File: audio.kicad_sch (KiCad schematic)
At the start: 36 parts, among them IC10 LM386

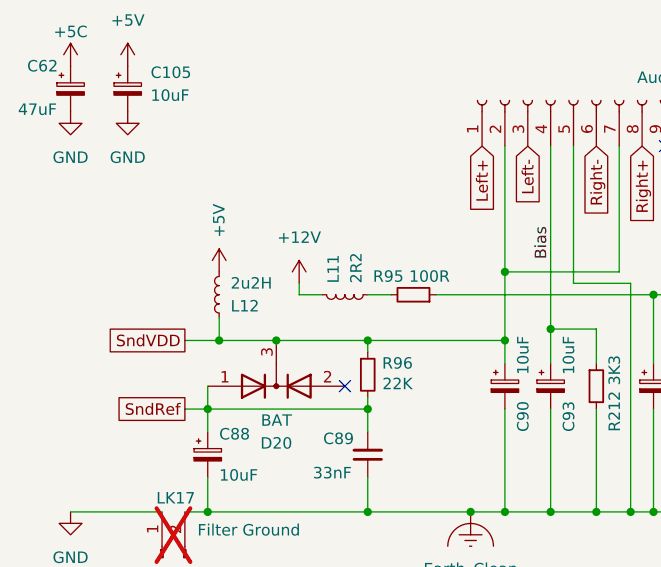
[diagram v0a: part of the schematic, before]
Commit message: fix incorrect value for L12
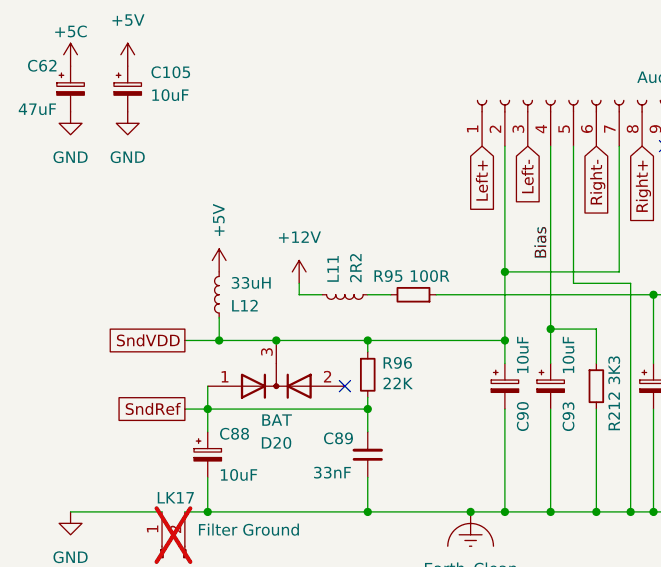
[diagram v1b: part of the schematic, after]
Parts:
- L12: value 2u2H -> 33uH
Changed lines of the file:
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@@
 			)
 		)
-		(property "Value" "2u2H"
+		(property "Value" "33uH"
 			(at 81.28 96.5201 0)
 			(effects

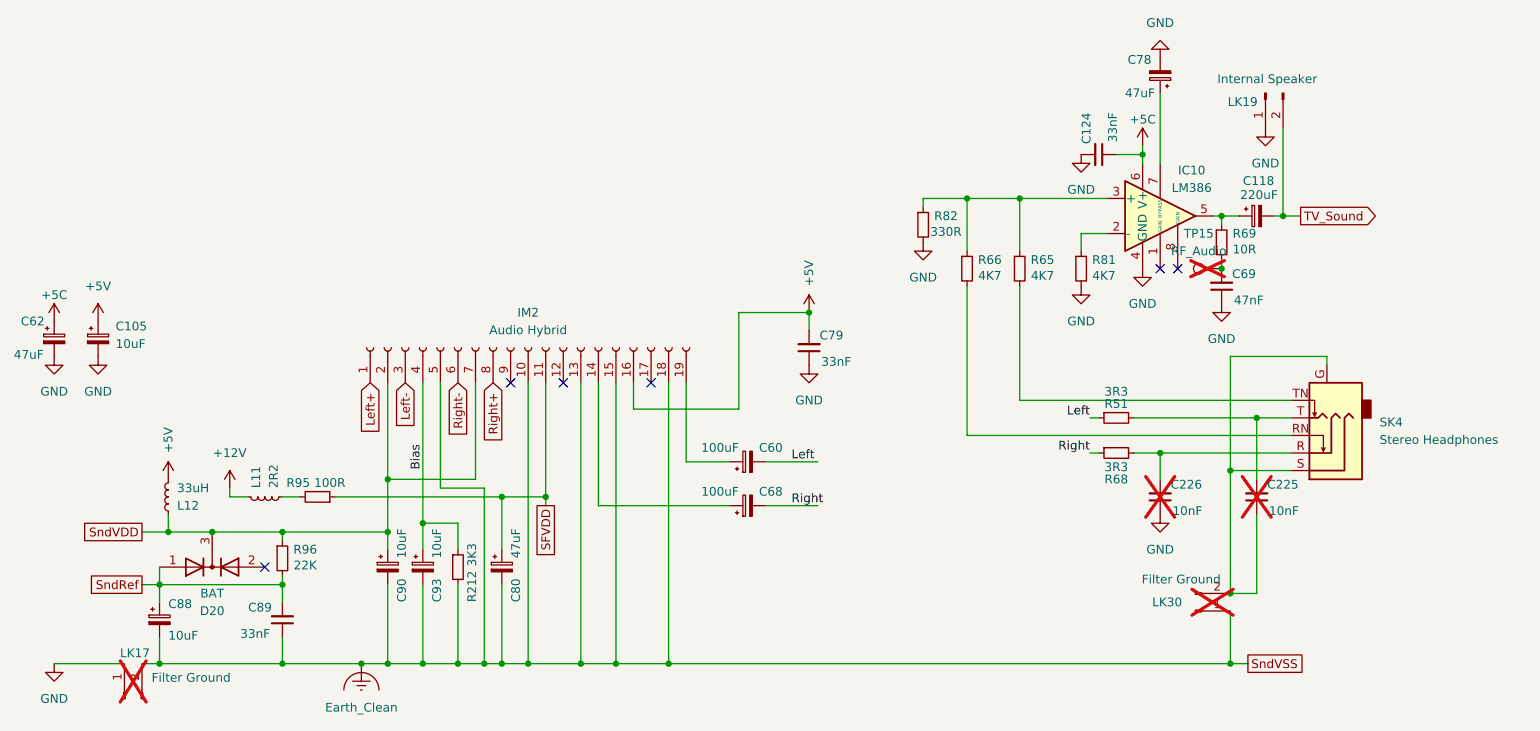
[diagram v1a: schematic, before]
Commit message: verify all component values vs TRM
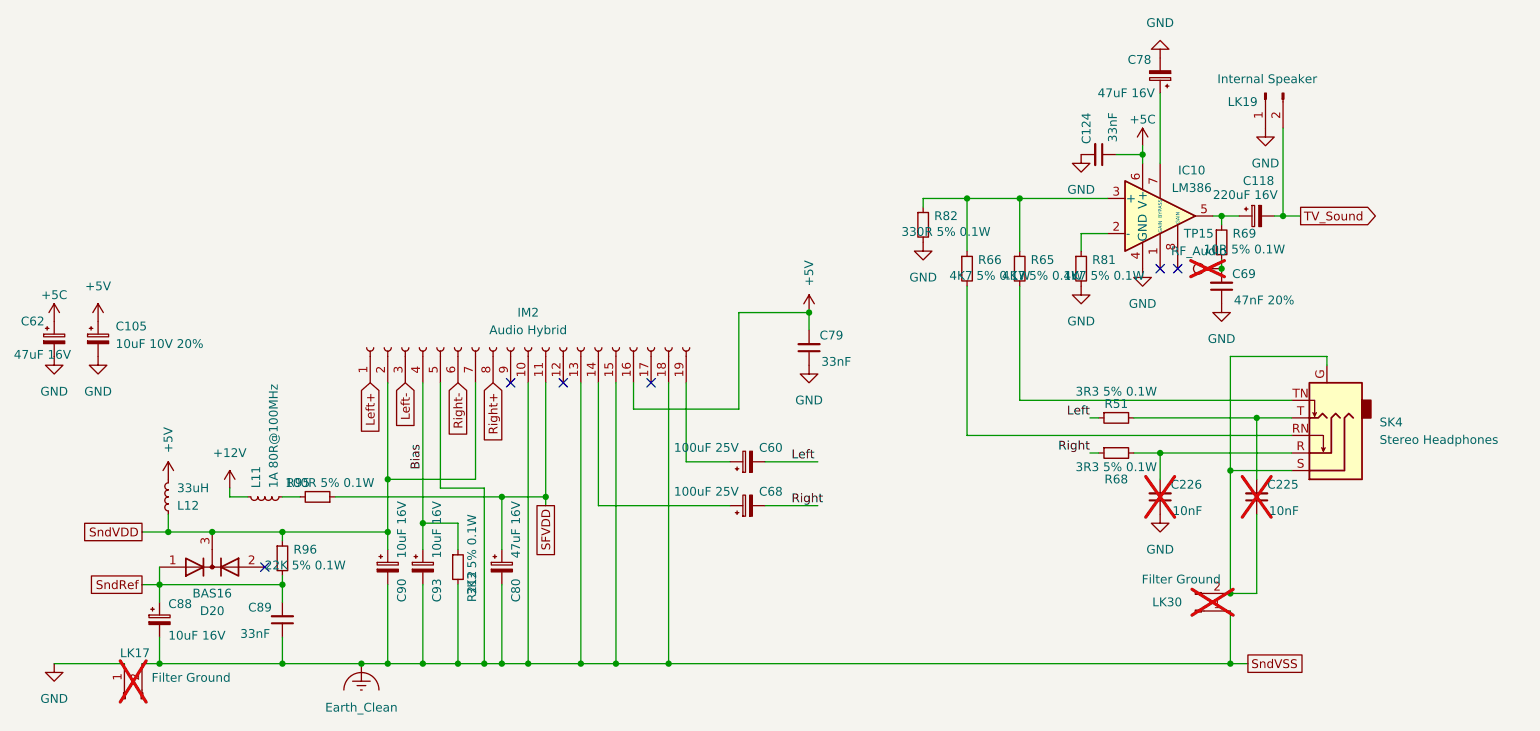
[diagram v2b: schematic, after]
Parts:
- C105: value 10uF -> 10uF 10V 20%
- C118: value 220uF -> 220uF 16V
- C60, C68: value 100uF -> 100uF 25V
- C62, C78, C80: value 47uF -> 47uF 16V
- C69: value 47nF -> 47nF 20%
- C88, C90, C93: value 10uF -> 10uF 16V
- D20: value BAT -> BAS16
- L11: value 2R2 -> 1A 80R@100MHz
- R212: value 3K3 -> 3K3 5% 0.1W
- R51, R68: value 3R3 -> 3R3 5% 0.1W
- R65, R66, R81: value 4K7 -> 4K7 5% 0.1W
- R69: value 10R -> 10R 5% 0.1W
- R82: value 330R -> 330R 5% 0.1W
- R95: value 100R -> 100R 5% 0.1W
- R96: value 22K -> 22K 5% 0.1W
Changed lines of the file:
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@@
 			)
 		)
-		(property "Value" "100uF"
+		(property "Value" "100uF 25V"
 			(at 162.56 90.678 90)
 			(effects
@@
 			)
 		)
-		(property "Value" "10uF"
+		(property "Value" "10uF 10V 20%"
 			(at 72.39 75.6538 0)
 			(effects
@@
 			)
 		)
-		(property "Value" "100uF"
+		(property "Value" "100uF 25V"
 			(at 162.56 97.028 90)
 			(effects
@@
 			)
 		)
-		(property "Value" "22K"
+		(property "Value" "22K 5% 0.1W"
 			(at 99.822 107.696 0)
 			(effects
@@
 			)
 		)
-		(property "Value" "47nF"
+		(property "Value" "47nF 20%"
 			(at 234.188 69.342 0)
 			(effects
@@
 			)
 		)
-		(property "Value" "100R"
+		(property "Value" "100R 5% 0.1W"
 			(at 103.378 95.758 90)
 			(effects
@@
 			)
 		)
-		(property "Value" "2R2"
+		(property "Value" "1A 80R@100MHz"
 			(at 95.2499 96.52 0)
 			(effects
@@
 			)
 		)
-		(property "Value" "4K7"
+		(property "Value" "4K7 5% 0.1W"
 			(at 206.502 65.786 0)
 			(effects
@@
 			)
 		)
-		(property "Value" "220uF"
+		(property "Value" "220uF 16V"
 			(at 240.538 54.102 90)
 			(effects
@@
 			)
 		)
-		(property "Value" "4K7"
+		(property "Value" "4K7 5% 0.1W"
 			(at 198.882 65.786 0)
 			(effects
@@
 			)
 		)
-		(property "Value" "3R3"
+		(property "Value" "3R3 5% 0.1W"
 			(at 217.17 82.55 90)
 			(effects
@@
 			)
 		)
-		(property "Value" "10uF"
+		(property "Value" "10uF 16V"
 			(at 80.01 117.856 0)
 			(effects
@@
 			)
 		)
-		(property "Value" "330R"
+		(property "Value" "330R 5% 0.1W"
 			(at 192.532 59.436 0)
 			(effects
@@
 			)
 		)
-		(property "Value" "47uF"
+		(property "Value" "47uF 16V"
 			(at 57.658 77.216 0)
 			(effects
@@
 			)
 		)
-		(property "Value" "10uF"
+		(property "Value" "10uF 16V"
 			(at 118.872 106.68 90)
 			(effects
@@
 			)
 		)
-		(property "Value" "3K3"
+		(property "Value" "3K3 5% 0.1W"
 			(at 123.952 106.172 90)
 			(effects
@@
 			)
 		)
-		(property "Value" "47uF"
+		(property "Value" "47uF 16V"
 			(at 130.302 106.68 90)
 			(effects
@@
 			)
 		)
-		(property "Value" "47uF"
+		(property "Value" "47uF 16V"
 			(at 222.758 39.37 0)
 			(effects
@@
 			)
 		)
-		(property "Value" "BAT"
+		(property "Value" "BAS16"
 			(at 86.36 111.76 0)
 			(effects
@@
 			)
 		)
-		(property "Value" "10R"
+		(property "Value" "10R 5% 0.1W"
 			(at 235.712 61.976 0)
 			(effects
@@
 			)
 		)
-		(property "Value" "10uF"
+		(property "Value" "10uF 16V"
 			(at 113.792 106.68 90)
 			(effects
@@
 			)
 		)
-		(property "Value" "3R3"
+		(property "Value" "3R3 5% 0.1W"
 			(at 217.17 93.472 90)
 			(effects
@@
 			)
 		)
-		(property "Value" "4K7"
+		(property "Value" "4K7 5% 0.1W"
 			(at 215.392 65.786 0)
 			(effects

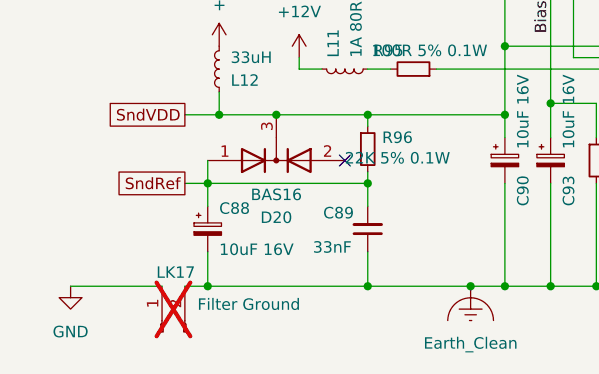
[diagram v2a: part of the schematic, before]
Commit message: switch links to net ties
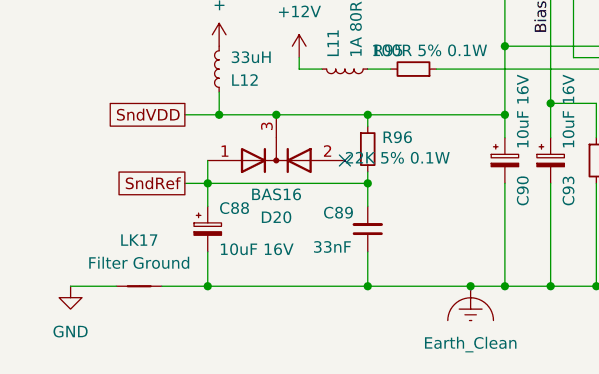
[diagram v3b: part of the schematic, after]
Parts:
- removed LK17: Filter Ground, Connector_PinHeader_2.54mm:PinHeader_1x02_P2.54mm_Vertical, symbol Connector:Conn_01x02_Pin
- added LK17: Filter Ground, Acorn:Link_Connected, symbol Device:NetTie_2
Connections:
- net Earth_Clean: now also LK17.2
- net GND: now also LK17.1
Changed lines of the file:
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@@
 	(wire
 		(pts
-			(xy 76.2 121.92) (xy 78.74 121.92)
+			(xy 73.66 121.92) (xy 78.74 121.92)
 		)
 		(stroke
@@
 	(wire
 		(pts
-			(xy 63.5 121.92) (xy 73.66 121.92)
+			(xy 63.5 121.92) (xy 68.58 121.92)
 		)
 		(stroke
@@
 	)
 	(symbol
-		(lib_id "Connector:Conn_01x02_Pin")
-		(at 73.66 127 90)
-		(unit 1)
-		(exclude_from_sim no)
-		(in_bom yes)
-		(on_board yes)
-		(dnp yes)
-		(property "Reference" "LK17"
-			(at 75.184 120.396 90)
-			(effects
-				(font
-					(size 1.27 1.27)
-				)
-			)
-		)
-		(property "Value" "Filter Ground"
-			(at 83.312 123.952 90)
-			(effects
-				(font
-					(size 1.27 1.27)
-				)
-			)
-		)
-		(property "Footprint" "Connector_PinHeader_2.54mm:PinHeader_1x02_P2.54mm_Vertical"
-			(at 73.66 127 0)
-			(effects
-				(font
-					(size 1.27 1.27)
-				)
-				(hide yes)
-			)
-		)
-		(property "Datasheet" "~"
-			(at 73.66 127 0)
-			(effects
-				(font
-					(size 1.27 1.27)
-				)
-				(hide yes)
-			)
-		)
-		(property "Description" "Generic connector, single row, 01x02, script generated"
-			(at 73.66 127 0)
-			(effects
-				(font
-					(size 1.27 1.27)
-				)
-				(hide yes)
-			)
-		)
-		(pin "2"
-		)
-		(pin "1"
-		)
-		(instances
-			(project "Acorn-A3010"
-				(path "/999882f3-94f8-4a89-9093-27a47d0cb289/0f9e4e4c-7eae-43dc-ad37-0c70003f4236"
-					(reference "LK17")
-					(unit 1)
-				)
-			)
-		)
-	)
-	(symbol
 		(lib_id "power:Earth_Clean")
 		(at 107.95 121.92 0)
@@
 					(unit 1)
 				)
+			)
+		)
+	)
+	(symbol
+		(lib_id "Device:NetTie_2")
+		(at 71.12 121.92 0)
+		(unit 1)
+		(exclude_from_sim no)
+		(in_bom no)
+		(on_board yes)
+		(dnp no)
+		(fields_autoplaced yes)
+		(property "Reference" "LK17"
+			(at 71.12 116.84 0)
+			(effects
+				(font
+					(size 1.27 1.27)
+				)
+			)
+		)
+		(property "Value" "Filter Ground"
+			(at 71.12 119.38 0)
+			(effects
+				(font
+					(size 1.27 1.27)
+				)
+			)
+		)
+		(property "Footprint" "Acorn:Link_Connected"
+			(at 71.12 121.92 0)
+			(effects
+				(font
+					(size 1.27 1.27)
+				)
+				(hide yes)
+			)
+		)
+		(property "Datasheet" "~"
+			(at 71.12 121.92 0)
+			(effects
+				(font
+					(size 1.27 1.27)
+				)
+				(hide yes)
+			)
+		)
+		(property "Description" "Net tie, 2 pins"
+			(at 71.12 121.92 0)
+			(effects
+				(font
+					(size 1.27 1.27)
+				)
+				(hide yes)
+			)
+		)
+		(pin "2"
+		)
+		(pin "1"
+		)
+		(instances
+			(project "Acorn-A3010"
+				(path "/999882f3-94f8-4a89-9093-27a47d0cb289/0f9e4e4c-7eae-43dc-ad37-0c70003f4236"
+					(reference "LK17")
+					(unit 1)
+				)

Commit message: fix power domain links with net ties
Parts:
- removed LK30: Filter Ground, Connector_PinHeader_2.54mm:PinHeader_1x02_P2.54mm_Vertical, symbol Connector:Conn_01x02_Pin
- added LK30: Filter Ground, Acorn:Link_Connected, symbol Device:NetTie_2
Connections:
- net Earth_Clean: now also LK30.1
- net at C225.1, SK4.G, SK4.S: now also LK30.2
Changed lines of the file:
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@@
 	)
 	(junction
+		(at 233.68 121.92)
+		(diameter 0)
+		(color 0 0 0 0)
+	)
+	(junction
 		(at 116.84 121.92)
 		(diameter 0)
@@
 	)
 	(junction
-		(at 233.68 121.92)
-		(diameter 0)
-		(color 0 0 0 0)
-	)
-	(junction
 		(at 233.68 93.98)
 		(diameter 0)
@@
 	(wire
 		(pts
-			(xy 233.68 121.92) (xy 233.68 114.3)
-		)
-		(stroke
-			(width 0)
-			(type default)
-		)
-	)
-	(wire
-		(pts
 			(xy 78.74 107.95) (xy 78.74 110.49)
 		)
@@
 	(wire
 		(pts
+			(xy 233.68 114.3) (xy 233.68 111.76)
+		)
+		(stroke
+			(width 0)
+			(type default)
+		)
+	)
+	(wire
+		(pts
 			(xy 195.58 54.61) (xy 195.58 62.23)
 		)
@@
 	(wire
 		(pts
+			(xy 233.68 121.92) (xy 236.22 121.92)
+		)
+		(stroke
+			(width 0)
+			(type default)
+		)
+	)
+	(wire
+		(pts
 			(xy 154.94 81.28) (xy 154.94 92.71)
 		)
@@
 	(wire
 		(pts
-			(xy 223.52 39.37) (xy 223.52 49.53)
+			(xy 233.68 119.38) (xy 233.68 121.92)
 		)
 		(stroke
@@
 	(wire
 		(pts
-			(xy 116.84 81.28) (xy 116.84 101.6)
+			(xy 223.52 39.37) (xy 223.52 49.53)
 		)
 		(stroke
@@
 	(wire
 		(pts
-			(xy 76.2 110.49) (xy 78.74 110.49)
+			(xy 116.84 81.28) (xy 116.84 101.6)
 		)
 		(stroke
@@
 	(wire
 		(pts
-			(xy 134.62 81.28) (xy 134.62 97.79)
+			(xy 76.2 110.49) (xy 78.74 110.49)
 		)
 		(stroke
@@
 	(wire
 		(pts
-			(xy 231.14 57.15) (xy 232.41 57.15)
+			(xy 134.62 81.28) (xy 134.62 97.79)
 		)
 		(stroke
@@
 	(wire
 		(pts
-			(xy 116.84 121.92) (xy 121.92 121.92)
+			(xy 231.14 57.15) (xy 232.41 57.15)
 		)
 		(stroke
@@
 	(wire
 		(pts
-			(xy 76.2 102.87) (xy 80.01 102.87)
+			(xy 116.84 121.92) (xy 121.92 121.92)
 		)
 		(stroke
@@
 	(wire
 		(pts
-			(xy 233.68 121.92) (xy 236.22 121.92)
+			(xy 76.2 102.87) (xy 80.01 102.87)
 		)
 		(stroke
@@
 	)
 	(symbol
-		(lib_id "Connector:Conn_01x02_Pin")
-		(at 228.6 114.3 0)
-		(mirror x)
-		(unit 1)
-		(exclude_from_sim no)
-		(in_bom yes)
-		(on_board yes)
-		(dnp yes)
-		(property "Reference" "LK30"
-			(at 224.536 113.03 0)
-			(effects
-				(font
-					(size 1.27 1.27)
-				)
-			)
-		)
-		(property "Value" "Filter Ground"
-			(at 226.568 109.728 0)
-			(effects
-				(font
-					(size 1.27 1.27)
-				)
-			)
-		)
-		(property "Footprint" "Connector_PinHeader_2.54mm:PinHeader_1x02_P2.54mm_Vertical"
-			(at 228.6 114.3 0)
-			(effects
-				(font
-					(size 1.27 1.27)
-				)
-				(hide yes)
-			)
-		)
-		(property "Datasheet" "~"
-			(at 228.6 114.3 0)
-			(effects
-				(font
-					(size 1.27 1.27)
-				)
-				(hide yes)
-			)
-		)
-		(property "Description" "Generic connector, single row, 01x02, script generated"
-			(at 228.6 114.3 0)
-			(effects
-				(font
-					(size 1.27 1.27)
-				)
-				(hide yes)
-			)
-		)
-		(pin "2"
-		)
-		(pin "1"
-		)
-		(instances
-			(project "Acorn-A3010"
-				(path "/999882f3-94f8-4a89-9093-27a47d0cb289/0f9e4e4c-7eae-43dc-ad37-0c70003f4236"
-					(reference "LK30")
-					(unit 1)
-				)
-			)
-		)
-	)
-	(symbol
 		(lib_id "Device:C_Polarized_Small")
 		(at 223.52 36.83 180)
@@
 					(unit 1)
 				)
+			)
+		)
+	)
+	(symbol
+		(lib_id "Device:NetTie_2")
+		(at 233.68 116.84 90)
+		(unit 1)
+		(exclude_from_sim no)
+		(in_bom no)
+		(on_board yes)
+		(dnp no)
+		(fields_autoplaced yes)
+		(property "Reference" "LK30"
+			(at 234.95 115.5699 90)
+			(effects
+				(font
+					(size 1.27 1.27)
+				)
+				(justify right)
+			)
+		)
+		(property "Value" "Filter Ground"
+			(at 234.95 118.1099 90)
+			(effects
+				(font
+					(size 1.27 1.27)
+				)
+				(justify right)
+			)
+		)
+		(property "Footprint" "Acorn:Link_Connected"
+			(at 233.68 116.84 0)
+			(effects
+				(font
+					(size 1.27 1.27)
+				)
+				(hide yes)
+			)
+		)
+		(property "Datasheet" "~"
+			(at 233.68 116.84 0)
+			(effects
+				(font
+					(size 1.27 1.27)
+				)
+				(hide yes)
+			)
+		)
+		(property "Description" "Net tie, 2 pins"
+			(at 233.68 116.84 0)
+			(effects
+				(font
+					(size 1.27 1.27)
+				)
+				(hide yes)
+			)
+		)
+		(pin "1"
+		)
+		(pin "2"
+		)
+		(instances
+			(project "Acorn-A3010"
+				(path "/999882f3-94f8-4a89-9093-27a47d0cb289/0f9e4e4c-7eae-43dc-ad37-0c70003f4236"
+					(reference "LK30")
+					(unit 1)
+				)

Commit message: correction to audio socket ground
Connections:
- net GND: now also C225.1, LK30.2, SK4.G, SK4.S
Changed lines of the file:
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@@
 	(wire
 		(pts
-			(xy 237.49 111.76) (xy 233.68 111.76)
+			(xy 223.52 111.76) (xy 233.68 111.76)
 		)
 		(stroke
@@
 	(wire
 		(pts
-			(xy 166.37 99.06) (xy 173.99 99.06)
+			(xy 166.37 99.06) (xy 170.18 99.06)
 		)
 		(stroke
@@
 	(wire
 		(pts
-			(xy 166.37 92.71) (xy 173.99 92.71)
+			(xy 166.37 92.71) (xy 170.18 92.71)
 		)
 		(stroke
@@
 	(wire
 		(pts
-			(xy 237.49 100.33) (xy 237.49 111.76)
+			(xy 96.52 102.87) (xy 111.76 102.87)
 		)
 		(stroke
@@
 	(wire
 		(pts
-			(xy 96.52 102.87) (xy 111.76 102.87)
+			(xy 232.41 57.15) (xy 234.95 57.15)
 		)
 		(stroke
@@
 	(wire
 		(pts
-			(xy 232.41 57.15) (xy 234.95 57.15)
+			(xy 210.82 48.26) (xy 212.09 48.26)
 		)
 		(stroke
@@
 	(symbol
 		(lib_id "power:GND")
-		(at 212.09 48.26 0)
+		(at 210.82 48.26 0)
 		(unit 1)
 		(exclude_from_sim no)
@@
 		(fields_autoplaced yes)
 		(property "Reference" "#PWR0206"
-			(at 212.09 54.61 0)
+			(at 210.82 54.61 0)
 			(effects
 				(font
@@
 		)
 		(property "Value" "GND"
-			(at 212.09 53.34 0)
+			(at 210.82 53.34 0)
 			(effects
 				(font
@@
 		)
 		(property "Footprint" ""
-			(at 212.09 48.26 0)
+			(at 210.82 48.26 0)
 			(effects
 				(font
@@
 		)
 		(property "Datasheet" ""
-			(at 212.09 48.26 0)
+			(at 210.82 48.26 0)
 			(effects
 				(font
@@
 		)
 		(property "Description" "Power symbol creates a global label with name \"GND\" , ground"
-			(at 212.09 48.26 0)
+			(at 210.82 48.26 0)
 			(effects
 				(font
@@
 	)
 	(symbol
+		(lib_id "power:GND")
+		(at 237.49 100.33 0)
+		(unit 1)
+		(exclude_from_sim no)
+		(in_bom yes)
+		(on_board yes)
+		(dnp no)
+		(fields_autoplaced yes)
+		(property "Reference" "#PWR0339"
+			(at 237.49 106.68 0)
+			(effects
+				(font
+					(size 1.27 1.27)
+				)
+				(hide yes)
+			)
+		)
+		(property "Value" "GND"
+			(at 237.49 105.41 0)
+			(effects
+				(font
+					(size 1.27 1.27)
+				)
+			)
+		)
+		(property "Footprint" ""
+			(at 237.49 100.33 0)
+			(effects
+				(font
+					(size 1.27 1.27)
+				)
+				(hide yes)
+			)
+		)
+		(property "Datasheet" ""
+			(at 237.49 100.33 0)
+			(effects
+				(font
+					(size 1.27 1.27)
+				)
+				(hide yes)
+			)
+		)
+		(property "Description" "Power symbol creates a global label with name \"GND\" , ground"
+			(at 237.49 100.33 0)
+			(effects
+				(font
+					(size 1.27 1.27)
+				)
+				(hide yes)
+			)
+		)
+		(pin "1"
+		)
+		(instances
+			(project "Acorn-A3010"
+				(path "/999882f3-94f8-4a89-9093-27a47d0cb289/0f9e4e4c-7eae-43dc-ad37-0c70003f4236"
+					(reference "#PWR0339")
+					(unit 1)
+				)
+			)
+		)
+	)
+	(symbol
 		(lib_id "Device:R_Small")
 		(at 189.23 58.42 0)
@@
 					(unit 1)
 				)
+			)
+		)
+	)
+	(symbol
+		(lib_id "power:GND")
+		(at 223.52 111.76 0)
+		(unit 1)
+		(exclude_from_sim no)
+		(in_bom yes)
+		(on_board yes)
+		(dnp no)
+		(fields_autoplaced yes)
+		(property "Reference" "#PWR0340"
+			(at 223.52 118.11 0)
+			(effects
+				(font
+					(size 1.27 1.27)
+				)
+				(hide yes)
+			)
+		)
+		(property "Value" "GND"
+			(at 223.52 116.84 0)
+			(effects
+				(font
+					(size 1.27 1.27)
+				)
+			)
+		)
+		(property "Footprint" ""
+			(at 223.52 111.76 0)
+			(effects
+				(font
+					(size 1.27 1.27)
+				)
+				(hide yes)
+			)
+		)
+		(property "Datasheet" ""
+			(at 223.52 111.76 0)
+			(effects
+				(font
+					(size 1.27 1.27)
+				)
+				(hide yes)
+			)
+		)
+		(property "Description" "Power symbol creates a global label with name \"GND\" , ground"
+			(at 223.52 111.76 0)
+			(effects
+				(font
+					(size 1.27 1.27)
+				)
+				(hide yes)
+			)
+		)
+		(pin "1"
+		)
+		(instances
+			(project "Acorn-A3010"
+				(path "/999882f3-94f8-4a89-9093-27a47d0cb289/0f9e4e4c-7eae-43dc-ad37-0c70003f4236"
+					(reference "#PWR0340")
+					(unit 1)
+				)
